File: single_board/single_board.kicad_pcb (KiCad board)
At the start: 4 copper layers, 80 x 80 mm, 118 parts, among them J1 CAN_OUT, J10 SWD, J11 SPI Debug, J12 Screw_Terminal_01x02, J13 Conn_01x03, J14 Conn_01x04, J15 Screw_Terminal_01x02, J16 UART, J17 BOOTSEL, J18 Conn_01x03, J19 Conn_01x04, J2 USB_C_Receptacle_USB2.0_16P, J20 Conn_01x03, J21 Screw_Terminal_01x02, J22 Conn_01x04, J23 Conn_01x03, J24 Conn_01x04, J25 Screw_Terminal_01x02, J26 Conn_01x03, J27 Conn_01x04, J3 Screw_Terminal_01x02, J4 Conn_01x02, J5 Screw_Terminal_01x02, J6 490107670612, J7 Screw_Terminal_01x02, J8 Conn_01x03, J9 Conn_01x04, Q1 AO3401A, Q2 AO3401A, Q3 AO3401A, Q4 AO3401A, Q5 2N7002, SW1 Button, U1 AP2112K-3.3, U2 TJA1042T-3, U3 USBLC6-2SC6, U4 LSM6DSV, U5 STM32G474VBTx, Y1 FC-135

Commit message: v3v3
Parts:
- moved C1 10.0 mm to (172.3, 136.0)
- moved C2 7.90 mm to (171.2, 136.0)
- moved C10 2.98 mm to (163.5, 138.3)
- moved C8 2.98 mm to (167.6, 146.0)
- moved C9 2.98 mm to (162.4, 138.3)
- moved J1 2.98 mm to (171.2, 149.8)
- moved R10 2.98 mm to (167.0, 144.2)
- moved R5 2.98 mm to (167.8, 143.1)
- moved R8 2.98 mm to (167.4, 141.4)
- moved U2 2.98 mm to (167.4, 136.6)
- moved D2 2.33 mm to (158.6, 126.0)
- moved D1 2.33 mm to (161.4, 126.1)
- moved R1 2.33 mm to (161.4, 129.3)
- moved R2 2.33 mm to (158.6, 129.3)
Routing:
- net v3v3: track 29.2 -> 372.4 mm
- net GND: track 55.3 -> 24.7 mm, vias 91 -> 89
- net 5V: track 83.0 -> 67.5 mm
- net /ENC4_B: track 46.3 -> 37.1 mm
- net /ENC5_B: track 41.7 -> 33.9 mm
- net /FDCAN_TX: track 23.9 -> 20.9 mm
- net /FDCAN_RX: track 21.0 -> 18.0 mm
- net /CAN_LED: track 12.3 -> 9.84 mm
- net /HEARTBEAT: track 11.8 -> 9.71 mm
- net /CAN_STB: track 39.6 -> 38.2 mm
- added copper zone on F.Cu, net /v3v3IN_debug

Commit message: 5v
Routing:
- net 5V: track 67.5 -> 196.3 mm

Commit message: Layout satisfactory
todo: vias, silkscreen
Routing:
- net 5V: track 196.3 -> 193.2 mm, vias 15 -> 16
- net v3v3: track 372.4 -> 373.3 mm
- net GND: vias 89 -> 163

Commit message: Merge
also fix idc footprint again
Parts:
- moved J6 0.07 mm to (176.4, 83.5)

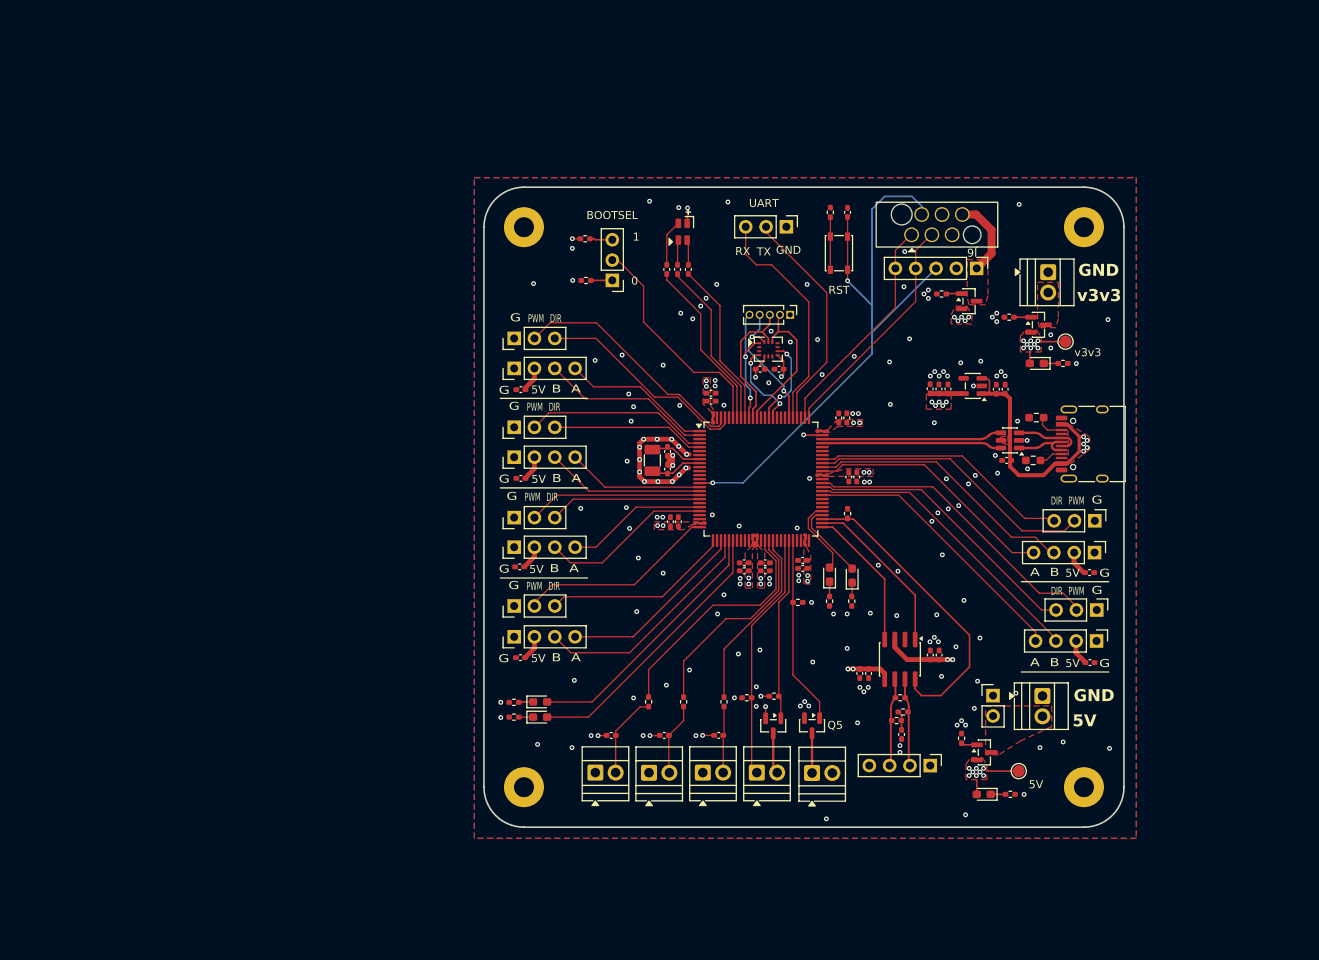
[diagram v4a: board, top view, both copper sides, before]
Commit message: Update Schematic
New footprints
Clean up schematic
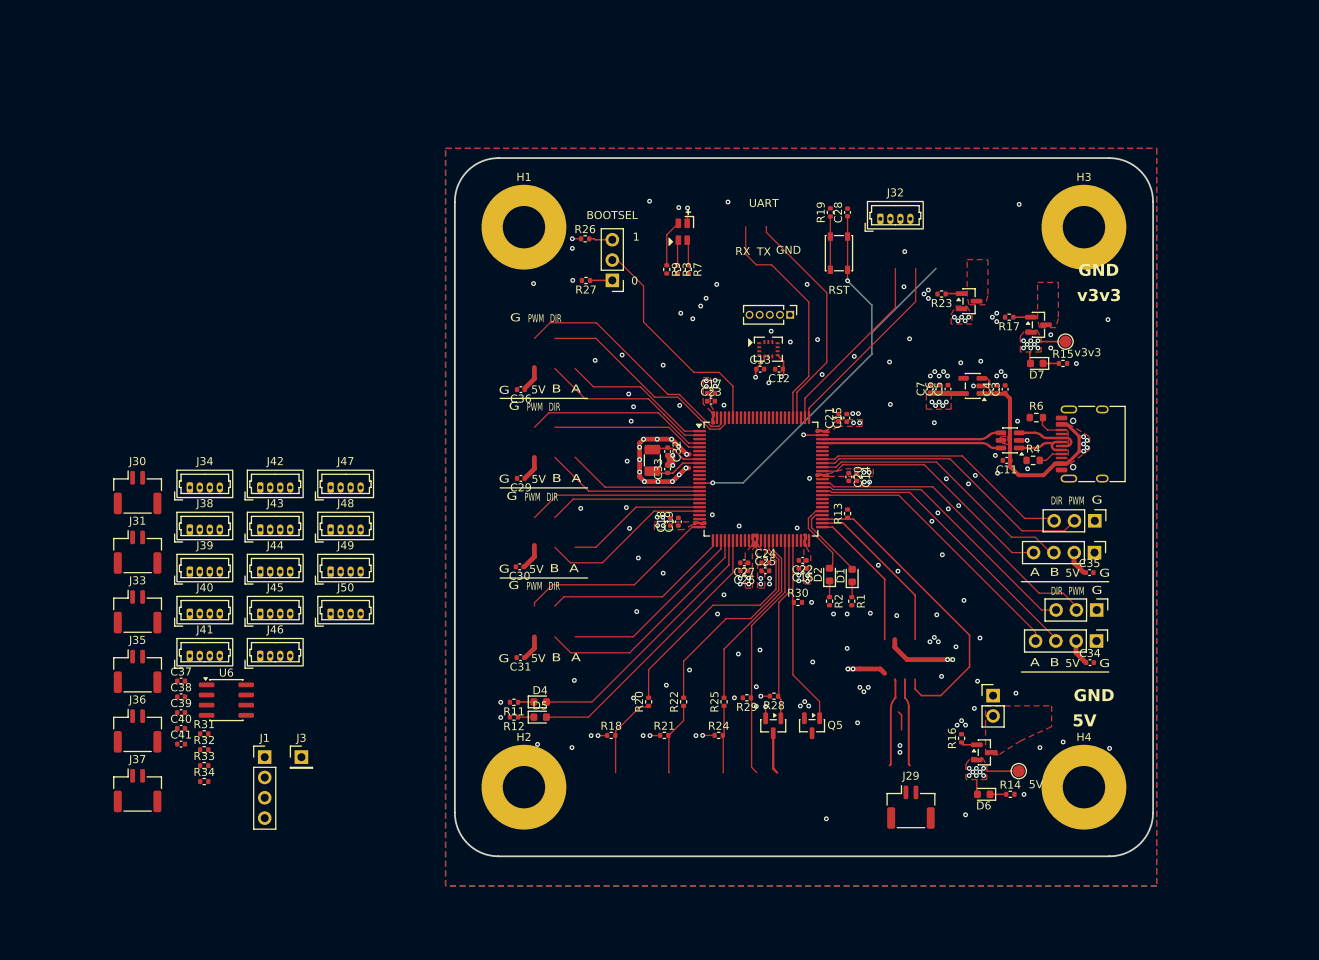
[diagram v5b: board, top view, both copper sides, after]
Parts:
- removed C1, C9: 1uF, Capacitor_SMD:C_0402_1005Metric_Pad0.74x0.62mm_HandSolder
- removed C10, C2: 100nF, Capacitor_SMD:C_0402_1005Metric_Pad0.74x0.62mm_HandSolder
- removed C8: 10nF, Capacitor_SMD:C_0402_1005Metric_Pad0.74x0.62mm_HandSolder
- removed J10: SWD, Connector_PinHeader_2.54mm:PinHeader_1x05_P2.54mm_Vertical
- removed J12, J15, J21, J25, J5, J7: Screw_Terminal_01x02, TerminalBlock:TerminalBlock_Xinya_XY308-2.54-2P_1x02_P2.54mm_Horizontal
- removed J13, J18, J26, J8: Conn_01x03, Connector_PinHeader_2.54mm:PinHeader_1x03_P2.54mm_Vertical
- removed J14, J19, J27, J9: Conn_01x04, Connector_PinHeader_2.54mm:PinHeader_1x04_P2.54mm_Vertical
- removed J16: UART, Connector_PinHeader_2.54mm:PinHeader_1x03_P2.54mm_Vertical
- removed J6: 490107670612, Rover:490107670612
- removed R10, R5: 60, Resistor_SMD:R_0402_1005Metric_Pad0.72x0.64mm_HandSolder
- removed R8: 120, Resistor_SMD:R_0402_1005Metric_Pad0.72x0.64mm_HandSolder
- removed U2: TJA1042T-3, Package_SO:SOIC-8_3.9x4.9mm_P1.27mm
- added C37: 1uF, Capacitor_SMD:C_0402_1005Metric, F.Cu at (77.5, 139.3)
- added C38: 100nF, Capacitor_SMD:C_0402_1005Metric, F.Cu at (77.5, 141.3)
- added C39: 1uF, Capacitor_SMD:C_0402_1005Metric, F.Cu at (77.5, 143.2)
- added C40: 100nF, Capacitor_SMD:C_0402_1005Metric, F.Cu at (77.5, 145.2)
- added C41: 10nF, Capacitor_SMD:C_0402_1005Metric, F.Cu at (77.5, 147.2)
- added J29: JST_GH_Horizontal, Connector_JST:JST_GH_SM02B-GHS-TB_1x02-1MP_P1.25mm_Horizontal, F.Cu at (168.8, 155.1)
- added J30: JST_GH_H, Connector_JST:JST_GH_SM02B-GHS-TB_1x02-1MP_P1.25mm_Horizontal, F.Cu at (72.1, 115.7)
- added J31: JST_GH_H, Connector_JST:JST_GH_SM02B-GHS-TB_1x02-1MP_P1.25mm_Horizontal, F.Cu at (72.1, 123.2)
- added J32: PB_Vertical, Connector_Molex:Molex_PicoBlade_53047-0410_1x04_P1.25mm_Vertical, F.Cu at (164.9, 81.5)
- added J33: JST_GH_H, Connector_JST:JST_GH_SM02B-GHS-TB_1x02-1MP_P1.25mm_Horizontal, F.Cu at (72.1, 130.6)
- added J34: PB_Vertical, Connector_Molex:Molex_PicoBlade_53047-0410_1x04_P1.25mm_Vertical, F.Cu at (78.6, 115.1)
- added J35: JST_GH_H, Connector_JST:JST_GH_SM02B-GHS-TB_1x02-1MP_P1.25mm_Horizontal, F.Cu at (72.1, 138.1)
- added J36: JST_GH_H, Connector_JST:JST_GH_SM02B-GHS-TB_1x02-1MP_P1.25mm_Horizontal, F.Cu at (72.1, 145.5)
- added J37: JST_GH_H, Connector_JST:JST_GH_SM02B-GHS-TB_1x02-1MP_P1.25mm_Horizontal, F.Cu at (72.1, 153.0)
- added J38: PB_Vertical, Connector_Molex:Molex_PicoBlade_53047-0410_1x04_P1.25mm_Vertical, F.Cu at (78.6, 120.3)
- added J39: PB_Vertical, Connector_Molex:Molex_PicoBlade_53047-0410_1x04_P1.25mm_Vertical, F.Cu at (78.6, 125.6)
- added J40: PB_Vertical, Connector_Molex:Molex_PicoBlade_53047-0410_1x04_P1.25mm_Vertical, F.Cu at (78.6, 130.9)
- added J41: PB_Vertical, Connector_Molex:Molex_PicoBlade_53047-0410_1x04_P1.25mm_Vertical, F.Cu at (78.6, 136.1)
- added J42: PB_Vertical, Connector_Molex:Molex_PicoBlade_53047-0410_1x04_P1.25mm_Vertical, F.Cu at (87.4, 115.1)
- added J43: PB_Vertical, Connector_Molex:Molex_PicoBlade_53047-0410_1x04_P1.25mm_Vertical, F.Cu at (87.4, 120.3)
- added J44: PB_Vertical, Connector_Molex:Molex_PicoBlade_53047-0410_1x04_P1.25mm_Vertical, F.Cu at (87.4, 125.6)
- added J45: PB_Vertical, Connector_Molex:Molex_PicoBlade_53047-0410_1x04_P1.25mm_Vertical, F.Cu at (87.4, 130.9)
- added J46: PB_Vertical, Connector_Molex:Molex_PicoBlade_53047-0410_1x04_P1.25mm_Vertical, F.Cu at (87.4, 136.1)
- added J47: PB_Vertical, Connector_Molex:Molex_PicoBlade_53047-0410_1x04_P1.25mm_Vertical, F.Cu at (96.2, 115.1)
- added J48: PB_Vertical, Connector_Molex:Molex_PicoBlade_53047-0410_1x04_P1.25mm_Vertical, F.Cu at (96.2, 120.3)
- added J49: PB_Vertical, Connector_Molex:Molex_PicoBlade_53047-0410_1x04_P1.25mm_Vertical, F.Cu at (96.2, 125.6)
- added J50: PB_Vertical, Connector_Molex:Molex_PicoBlade_53047-0410_1x04_P1.25mm_Vertical, F.Cu at (96.2, 130.9)
- added R31: 10k, Resistor_SMD:R_0402_1005Metric, F.Cu at (80.4, 145.9)
- added R32: 120, Resistor_SMD:R_0402_1005Metric, F.Cu at (80.4, 147.9)
- added R33: 60, Resistor_SMD:R_0402_1005Metric, F.Cu at (80.4, 149.9)
- added R34: 60, Resistor_SMD:R_0402_1005Metric, F.Cu at (80.4, 151.8)
- added U6: ~, Package_SO:SOIC-8_3.9x4.9mm_P1.27mm, F.Cu at (83.2, 141.7)
- C11, C12, C13, C14, C15, C16, C17, C18, C19, C20, C21, C22, C23, C24, C25, C26, C27, C28, C29, C3, C30, C31, C32, C33, C34, C35, C36, C4, C5, C6, C7: footprint Capacitor_SMD:C_0402_1005Metric_Pad0.74x0.62mm_HandSolder -> Capacitor_SMD:C_0402_1005Metric
- D1, D2, D4, D5, D6, D7: footprint LED_SMD:LED_0603_1608Metric_Pad1.05x0.95mm_HandSolder -> Diode_SMD:D_0603_1608Metric
- H1, H2, H3, H4: footprint MountingHole:MountingHole_2.5mm_Pad -> MountingHole:MountingHole_5.3mm_M5_Pad
- J1: value CAN_OUT -> SWD
- J3: value Screw_Terminal_01x02 -> RST; footprint TerminalBlock:TerminalBlock_Xinya_XY308-2.54-2P_1x02_P2.54mm_Horizontal -> Connector_PinHeader_2.54mm:PinHeader_1x01_P2.54mm_Vertical
- R1, R11, R12, R13, R14, R15, R16, R17, R19, R2, R20, R22, R23, R25, R26, R27, R28, R29, R30: footprint Resistor_SMD:R_0402_1005Metric_Pad0.72x0.64mm_HandSolder -> Resistor_SMD:R_0402_1005Metric
- R18, R21, R24, R3, R7, R9: footprint Capacitor_SMD:C_0402_1005Metric_Pad0.74x0.62mm_HandSolder -> Resistor_SMD:R_0402_1005Metric
- R4, R6: footprint Resistor_SMD:R_0603_1608Metric_Pad0.98x0.95mm_HandSolder -> Resistor_SMD:R_0603_1608Metric
- moved J3 92.9 mm to (92.6, 148.8), turned to 0 degrees
- moved J1 83.2 mm to (88.0, 148.8), turned to 0 degrees
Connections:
- J1 pad 1: GND -> /v3v3IN_debug
- J1 pad 2: /can_DP -> GND
- J1 pad 3: /can_DN -> /SWDIO
- J1 pad 4: GND -> /SWCLK
- J3 pad 1: GND -> /RST
- R20 pad 2: /LS1 -> /L_SW1
- R22 pad 2: /LS2 -> /L_SW2
- R25 pad 2: /LS3 -> /L_SW3
- U5 pad 39: /LS1 -> unconnected-(U5-PE8-Pad39)
- U5 pad 40: /LS2 -> unconnected-(U5-PE9-Pad40)
- U5 pad 41: /LS3 -> /L_SW1
- U5 pad 42: unconnected-(U5-PE11-Pad42) -> /L_SW2
- U5 pad 43: unconnected-(U5-PE12-Pad43) -> /L_SW3
- U5 pad 51: /FDCAN_RX -> /CAN_RX
- U5 pad 52: /FDCAN_TX -> /CAN_TX
- U5 pad 81: /IMU_MOSI -> /UART5_TX
- U5 pad 84: unconnected-(U5-PD2-Pad84) -> /UART5_RX
- U5 pad 85: /INT1 -> /TRI_LED_G
- U5 pad 86: /INT2 -> /TRI_LED_R
- U5 pad 87: unconnected-(U5-PD5-Pad87) -> /TRI_LED_B
- U5 pad 88: unconnected-(U5-PD6-Pad88) -> /INT2
- U5 pad 92: /TRI_LED_G -> /IMU_MOSI
- U5 pad 93: /TRI_LED_R -> /INT1
- U5 pad 94: /TRI_LED_B -> unconnected-(U5-PB7-Pad94)
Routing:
- net (no net): track 0.00 -> 47.4 mm
- net 5V: track 193.2 -> 152.5 mm
- net Earth: track 0.00 -> 40.7 mm
- net unconnected-(U5-PE8-Pad39): track 0.00 -> 30.2 mm
- net /LS1: track 30.2 -> 0.00 mm
- net unconnected-(U5-PE9-Pad40): track 0.00 -> 26.8 mm
- net /LS2: track 26.8 -> 0.00 mm
- net /LS3: track 23.0 -> 0.00 mm
- net /TRI_LED_B: track 21.6 -> 0.00 mm
- net /TRI_LED_R: track 21.2 -> 0.00 mm
- net /TRI_LED_G: track 20.9 -> 0.00 mm
- net /FDCAN_TX: track 20.9 -> 0.00 mm
- net /CAN_TX: track 0.00 -> 20.9 mm
- net /RST: track 78.4 -> 58.0 mm
- net /IMU_NSS: track 18.3 -> 0.00 mm
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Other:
- board size 80 x 80 mm -> 87.3 x 87.3 mm

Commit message: I2C, connectors
Update connectors, add I2C bus to MCU
TODO: routing new connectors
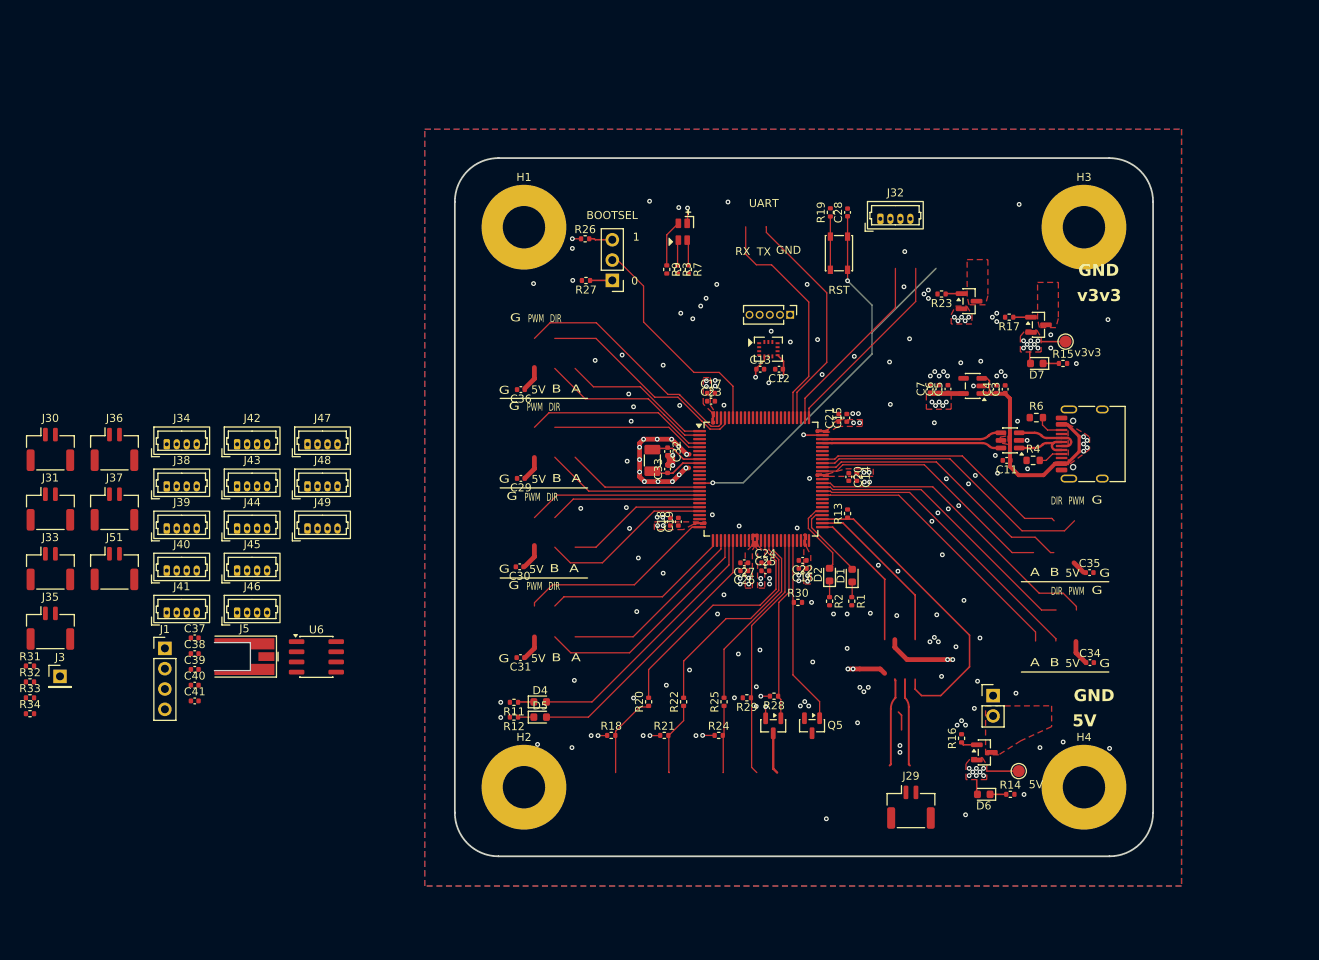
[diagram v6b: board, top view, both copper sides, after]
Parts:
- removed J20, J23: Conn_01x03, Connector_PinHeader_2.54mm:PinHeader_1x03_P2.54mm_Vertical
- removed J22, J24: Conn_01x04, Connector_PinHeader_2.54mm:PinHeader_1x04_P2.54mm_Vertical
- removed J50: PB_Vertical, Connector_Molex:Molex_PicoBlade_53047-0410_1x04_P1.25mm_Vertical
- added J5: Conn_01x02, Connector_Coaxial:MMCX_Molex_73415-0961_Horizontal_0.8mm-PCB, F.Cu at (85.5, 136.2)
- added J51: JST_GH_H, Connector_JST:JST_GH_SM02B-GHS-TB_1x02-1MP_P1.25mm_Horizontal, F.Cu at (69.2, 125.2)
- moved J36 35.3 mm to (69.2, 110.3)
- moved J37 35.3 mm to (69.2, 117.8)
- moved J3 31.8 mm to (62.4, 138.7)
- moved R32 23.4 mm to (58.7, 139.4)
- moved R31 23.4 mm to (58.7, 137.4)
- moved R33 23.4 mm to (58.7, 141.4)
- moved R34 23.4 mm to (58.7, 143.4)
- moved J1 18.5 mm to (75.5, 135.2)
- moved U6 12.5 mm to (94.5, 136.3)
- moved J33 12.2 mm to (61.2, 125.2)
- moved J30 12.2 mm to (61.2, 110.3)
- moved J31 12.2 mm to (61.2, 117.8)
- moved J35 12.2 mm to (61.2, 132.7)
- moved J38 6.12 mm to (75.7, 114.9)
- moved J39 6.12 mm to (75.7, 120.2)
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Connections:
- U5 pad 69: unconnected-(U5-PA8-Pad69) -> /I2C_SDA
- U5 pad 70: unconnected-(U5-PA9-Pad70) -> /I2C_SCL
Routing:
- net 5V: track 152.5 -> 151.1 mm

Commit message: Clear Routing
Clear previous routing, preparation for new picoblade and jst gh connectors
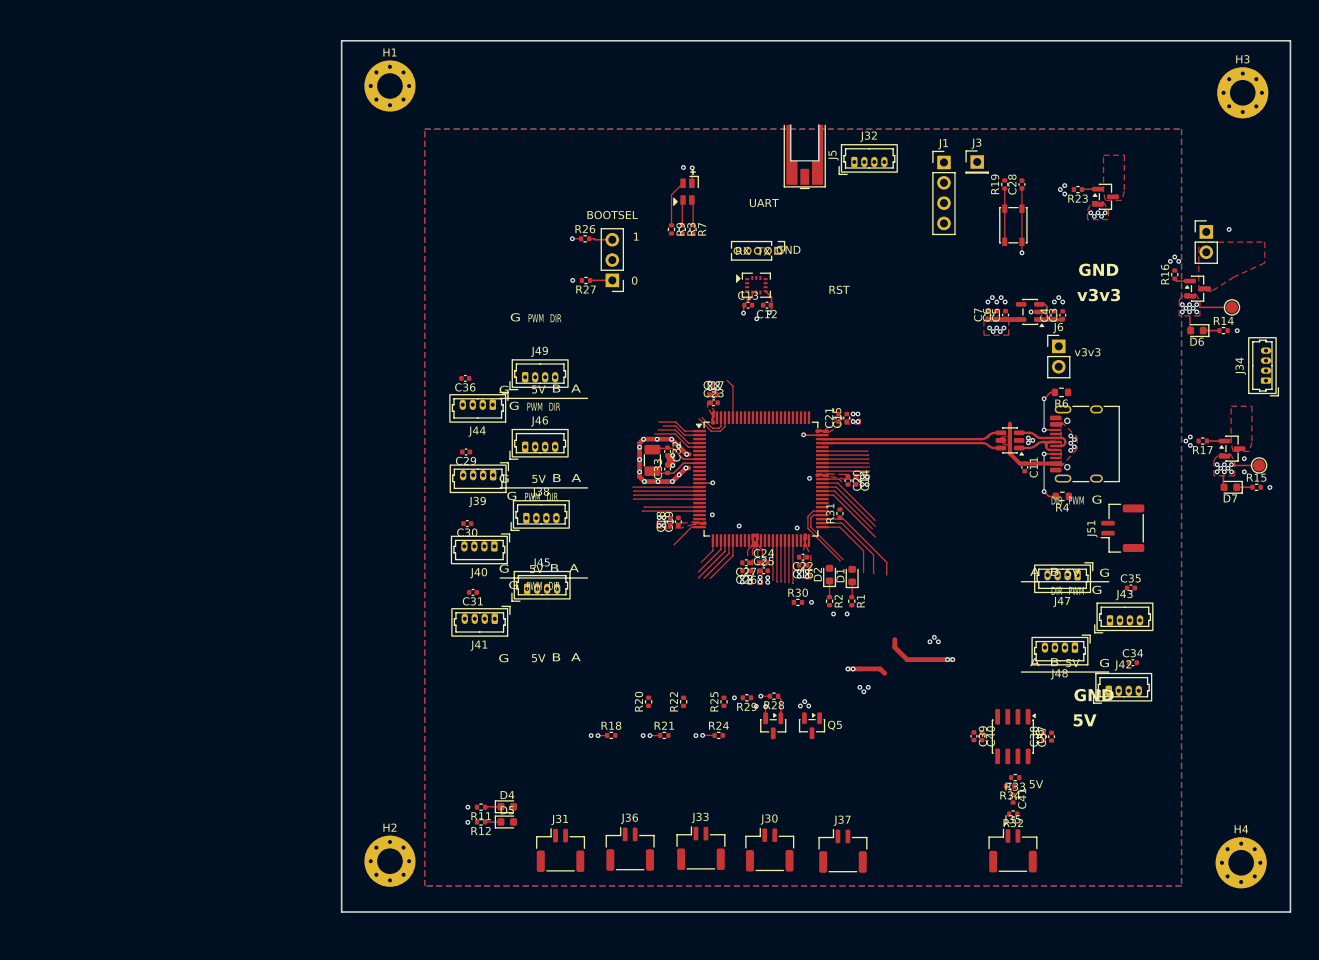
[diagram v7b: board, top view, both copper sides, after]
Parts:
- removed J29: JST_GH_Horizontal, Connector_JST:JST_GH_SM02B-GHS-TB_1x02-1MP_P1.25mm_Horizontal
- removed R13: 10k, Resistor_SMD:R_0402_1005Metric
- added J6: Conn_01x02, Connector_PinHeader_2.54mm:PinHeader_1x02_P2.54mm_Vertical, F.Cu at (187.2, 97.5)
- H1, H2, H3, H4: footprint MountingHole:MountingHole_5.3mm_M5_Pad -> MountingHole:MountingHole_3.2mm_M3_Pad_Via
- moved J34 137.6 mm to (213.2, 101.7), turned to 90 degrees
- moved J3 131.4 mm to (177.1, 74.4)
- moved J51 126.1 mm to (195.2, 120.2), turned to 90 degrees
- moved R32 124.0 mm to (181.6, 155.9), turned to 180 degrees
- moved R33 123.6 mm to (181.8, 151.3), turned to 180 degrees
- moved J35 123.5 mm to (181.5, 160.5)
- moved R34 122.8 mm to (181.2, 152.4), turned to 180 degrees
- moved J1 114.8 mm to (172.9, 74.5)
- moved J42 113.2 mm to (193.5, 140.5)
- moved J43 110.4 mm to (193.7, 131.7)
- moved C37 107.8 mm to (186.3, 146.2), turned to 90 degrees
- moved C38 106.6 mm to (185.3, 146.2), turned to 90 degrees
- moved C41 103.0 mm to (181.6, 154.0), turned to -90 degrees
- moved R31 103.0 mm to (159.9, 118.3), turned to 90 degrees
- moved J30 102.9 mm to (151.1, 160.4)
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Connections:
- C3 pad 1: 5V -> Net-(J6-Pin_1)
- C4 pad 1: 5V -> Net-(J6-Pin_1)
- H1 pad 1: Earth -> GND
- H2 pad 1: Earth -> GND
- H3 pad 1: Earth -> GND
- H4 pad 1: Earth -> GND
- J34 pad 1: /5VIN -> GND
- J34 pad 2: GND -> /5VIN
- J35 pad 1: /CAN_DP -> /CAN_DN
- J35 pad 2: /CAN_DN -> /CAN_DP
- U1 pad 1: 5V -> Net-(J6-Pin_1)
- U1 pad 3: 5V -> Net-(J6-Pin_1)
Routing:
- net v3v3: track 373.3 -> 29.6 mm
- net 5V: track 151.1 -> 26.5 mm
- net /RST: track 58.0 -> 9.65 mm
- net (no net): track 47.4 -> 0.00 mm
- net Earth: track 40.7 -> 0.00 mm
- net unconnected-(U5-PE8-Pad39): track 30.2 -> 0.00 mm
- net /PWM4: track 36.0 -> 5.84 mm
- net /PWM5: track 38.6 -> 8.53 mm
- net /UART4_RX: track 29.1 -> 0.00 mm
- net /ENC4_B: track 37.1 -> 8.21 mm
- net /LED2: track 34.7 -> 5.91 mm
- net /UART4_TX: track 28.6 -> 0.00 mm
- net /ENC5_B: track 33.9 -> 5.89 mm
- net /DIR5: track 35.6 -> 8.65 mm
- net /LED1: track 32.9 -> 6.03 mm
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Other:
- board size 87.3 x 87.3 mm -> 118.6 x 108.9 mm
